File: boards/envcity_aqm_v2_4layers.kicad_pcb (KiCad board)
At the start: 4 copper layers, 110 x 100 mm, 109 parts, among them IC1 DS1307ZN+, J1 217175-0001, J10 Conn_01x03_Male, J11 Conn_01x04_Male, J12 Conn_01x02_Male, J13 Conn_01x02_Male, J14 Micro_SD_Card, J2 Screw_Terminal_01x02, J3 Screw_Terminal_01x02, J4 Conn_01x06_Male, J5 Conn_01x06_Male, J6 Conn_01x06_Male, J7 Conn_01x06_Male, Q1 DMG2301L, Q10 BC808, Q11 BC808, Q12 DMG2301L / DMP2045U, Q13 DMN10H220L, Q14 DMN10H220L, Q2 DMG2301L, Q3 BC808, Q4 BC808, Q5 DMG2301L / DMP2045U, Q6 BC808, Q7 BC808, Q8 DMG2301L, Q9 DMG2301L / DMP2045U, U1 ADS1115IDGS, U2 CD74HC4067M, U3 Heltec_Wifi_LoRa_V2, U4 LM2596S-5, U5 TP4056, U6 MT3608, U7 MT3608, U8 DHT11, Y1 32,768KHz

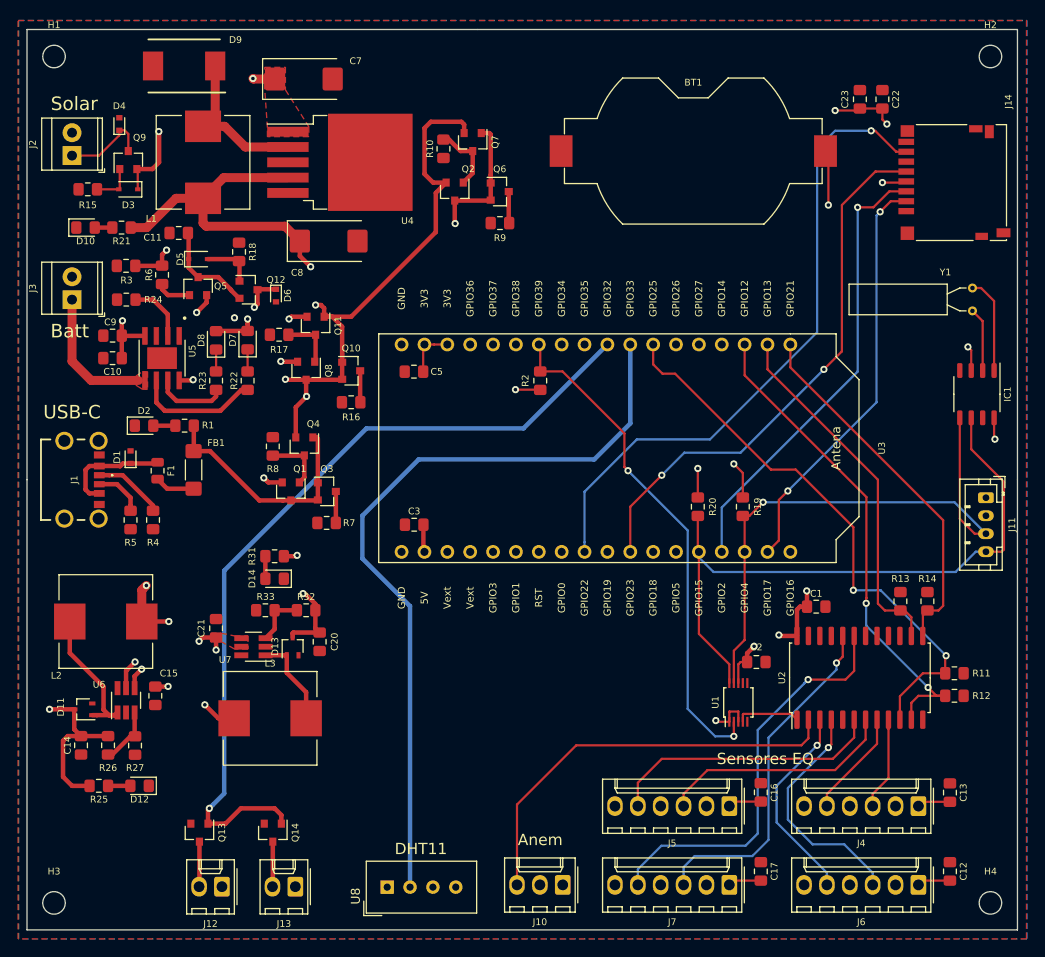
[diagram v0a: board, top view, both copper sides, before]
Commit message: Add placa com 4 camadas. Add dht11.
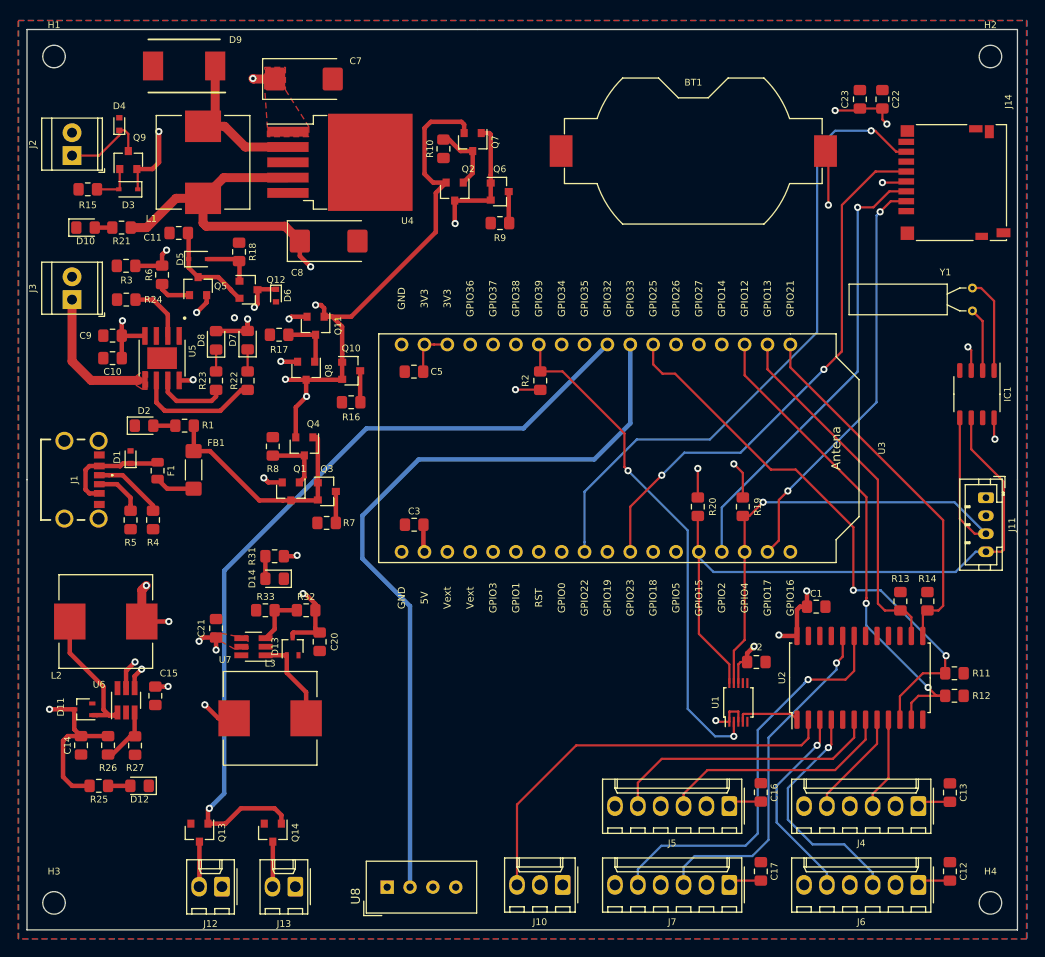
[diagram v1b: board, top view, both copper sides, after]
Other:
- board text removed: "Anem"
- board text removed: "Batt"
- board text removed: "DHT11"
- board text removed: "Sensores EQ"
- board text removed: "Solar"
- board text removed: "USB-C"
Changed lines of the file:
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@@
   (general
     (thickness 1.6)
-    (drawings 13)
+    (drawings 7)
     (tracks 607)
     (zones 0)
@@
     (tags "capacitor handsolder")
     (attr smd)
-    (fp_text reference C9 (at 0.25 1.5) (layer F.SilkS)
+    (fp_text reference C9 (at 3 0) (layer F.SilkS)
       (effects (font (size 0.75 0.75) (thickness 0.1)))
     )
@@
     )
   )
-  (gr_text "Sensores EQ" (at 193.5 141) (layer F.SilkS)
-    (effects (font (size 1.25 1.25) (thickness 0.1875)))
-  )
-  (gr_text Anem (at 168.5 150) (layer F.SilkS)
-    (effects (font (size 1.25 1.25) (thickness 0.1875)))
-  )
-  (gr_text DHT11 (at 155.25 151) (layer F.SilkS)
-    (effects (font (size 1.25 1.25) (thickness 0.1875)))
-  )
-  (gr_text Batt (at 116.25 93.5) (layer F.SilkS)
-    (effects (font (size 1.5 1.5) (thickness 0.3)))
-  )
-  (gr_text Solar (at 116.75 68.25) (layer F.SilkS)
-    (effects (font (size 1.5 1.5) (thickness 0.3)))
-  )
-  (gr_text USB-C (at 116.5 102.5) (layer F.SilkS)
-    (effects (font (size 1.5 1.5) (thickness 0.3)))
-  )
   (gr_line (start 111.5 160) (end 111.5 110) (layer Edge.Cuts) (width 0.05))
